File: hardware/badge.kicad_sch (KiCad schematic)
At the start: 53 parts, among them J1 SAO V.1.69bis master, Q1 BSS138, SW1 power, SW2 SW_Push, SW3 update epaper, U1 Seeed XIAO ESP32-C3, U2 MH-ET_epaper_ 2.13, U3 5V boost converter, U4 TXS0104EPWR

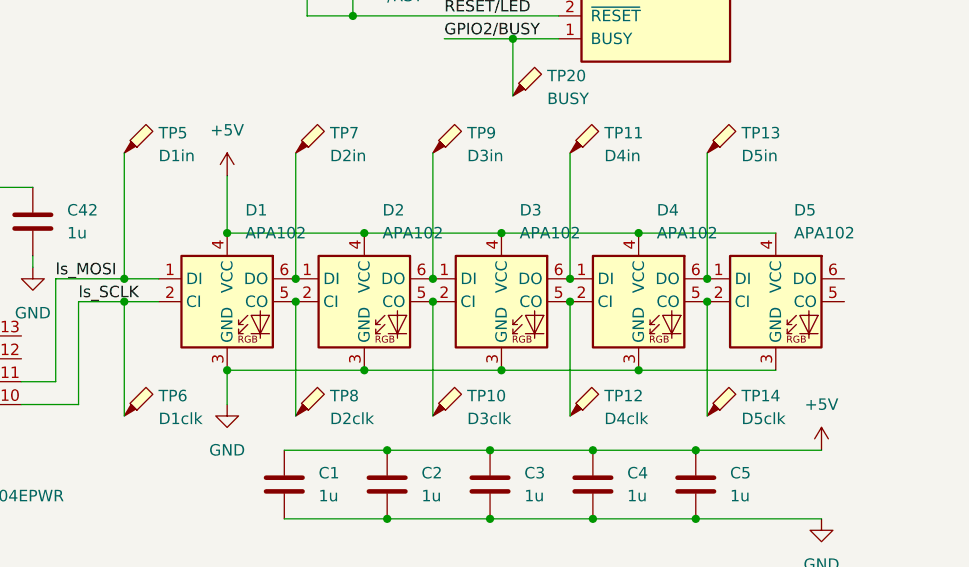
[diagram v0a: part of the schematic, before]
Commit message: fix smart LED APA102-2020, and some minor re-routings
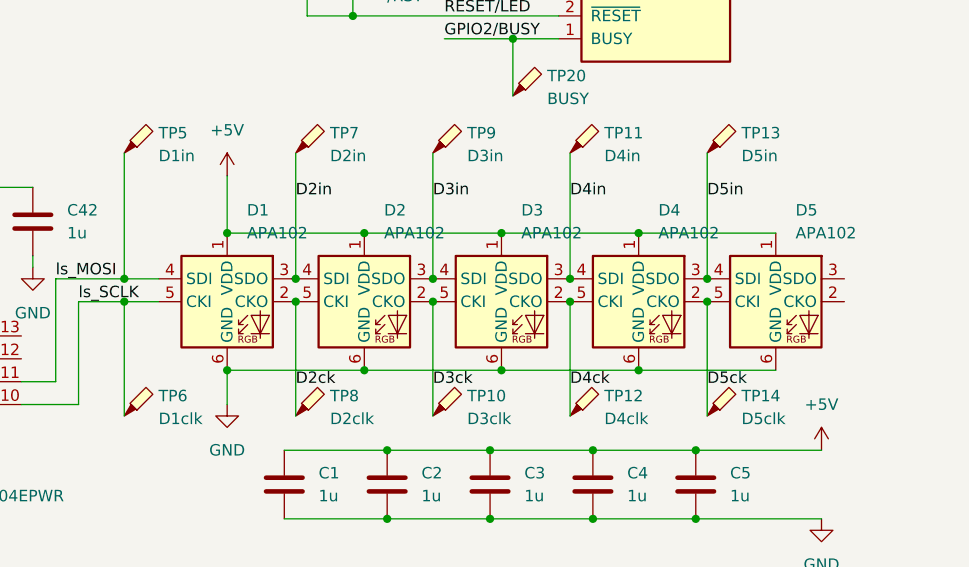
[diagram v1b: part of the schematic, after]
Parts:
- D1, D2, D3, D4, D5: footprint extra:LED-APA102-2020 -> LED_SMD:LED-APA102-2020; symbol LED:APA102 -> LED:APA102-2020
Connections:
- net +5V: now also D1.1 (VDD), D2.1 (VDD), D3.1 (VDD), D4.1 (VDD), D5.1 (VDD); no longer D1.4 (VCC), D2.4 (VCC), D3.4 (VCC), D4.4 (VCC), D5.4 (VCC)
- net GND: now also D1.6 (GND), D2.6 (GND), D3.6 (GND), D4.6 (GND), D5.6 (GND); no longer D1.3 (GND), D2.3 (GND), D3.3 (GND), D4.3 (GND), D5.3 (GND)
- net ls_MOSI: now also D1.4 (SDI); no longer D1.1 (DI)
- net ls_SCLK: now also D1.5 (CKI); no longer D1.2 (CI)
- net D5ck: now reaches D5.5 (CKI)
- net D5ck: now also D4.2 (CKO), TP14.1
- new net D2ck: D1.2 (CKO), D2.5 (CKI), TP8.1
- new net D2in: D1.3 (SDO), D2.4 (SDI), TP7.1
- new net D3ck: D2.2 (CKO), D3.5 (CKI), TP10.1
- new net D3in: D2.3 (SDO), D3.4 (SDI), TP9.1
- new net D4ck: D3.2 (CKO), D4.5 (CKI), TP12.1
- new net D4in: D3.3 (SDO), D4.4 (SDI), TP11.1
- new net D5in: D4.3 (SDO), D5.4 (SDI), TP13.1
- now unconnected: D5.2 (CI)
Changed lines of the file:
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@@
+    (effects (font (size 1.27 1.27)) (justify left bottom))
+  )
+  (label "D3ck" (at 229.87 98.425 0) (fields_autoplaced)
     (effects (font (size 1.27 1.27)) (justify left bottom))
   )
@@
     (effects (font (size 1.27 1.27)) (justify left bottom))
   )
+  (label "D2in" (at 214.63 77.47 0) (fields_autoplaced)
+    (effects (font (size 1.27 1.27)) (justify left bottom))
+  )
   (label "GPIO2{slash}BUSY" (at 266.7 135.89 0) (fields_autoplaced)
     (effects (font (size 1.27 1.27)) (justify left bottom))
@@
     (effects (font (size 1.27 1.27)) (justify left bottom))
   )
+  (label "D4ck" (at 245.11 98.425 0) (fields_autoplaced)
+    (effects (font (size 1.27 1.27)) (justify left bottom))
+  )
   (label "MOSI" (at 151.13 97.79 0) (fields_autoplaced)
     (effects (font (size 1.27 1.27)) (justify left bottom))
@@
     (effects (font (size 1.27 1.27)) (justify left bottom))
   )
+  (label "D2ck" (at 214.63 98.425 0) (fields_autoplaced)
+    (effects (font (size 1.27 1.27)) (justify left bottom))
+  )
+  (label "D5in" (at 260.35 77.47 0) (fields_autoplaced)
+    (effects (font (size 1.27 1.27)) (justify left bottom))
+  )
   (label "CS{slash}OE" (at 127 60.96 0) (fields_autoplaced)
     (effects (font (size 1.27 1.27)) (justify left bottom))
@@
     (effects (font (size 1.27 1.27)) (justify left bottom))
   )
+  (label "D4in" (at 245.11 77.47 0) (fields_autoplaced)
+    (effects (font (size 1.27 1.27)) (justify left bottom))
+  )
   (label "CS{slash}OE" (at 151.13 90.17 0) (fields_autoplaced)
     (effects (font (size 1.27 1.27)) (justify left bottom))
@@
     (effects (font (size 1.27 1.27)) (justify left bottom))
   )
+  (label "D3in" (at 229.87 77.47 0) (fields_autoplaced)
+    (effects (font (size 1.27 1.27)) (justify left bottom))
+  )
   (label "RESET{slash}LED" (at 59.69 60.96 0) (fields_autoplaced)
     (effects (font (size 1.27 1.27)) (justify left bottom))
   )
   (label "Vdark" (at 59.69 45.72 0) (fields_autoplaced)
+    (effects (font (size 1.27 1.27)) (justify left bottom))
+  )
+  (label "D5ck" (at 260.35 98.425 0) (fields_autoplaced)
     (effects (font (size 1.27 1.27)) (justify left bottom))
   )
@@
     )
   )
-  (symbol (lib_id "LED:APA102") (at 237.49 88.9 0) (unit 1)
-    (in_bom yes) (on_board yes) (dnp no) (fields_autoplaced)
-    (property "Reference" "D3" (at 239.5094 78.74 0)
-      (effects (font (size 1.27 1.27)) (justify left))
-    )
-    (property "Value" "APA102" (at 239.5094 81.28 0)
-      (effects (font (size 1.27 1.27)) (justify left))
-    )
-    (property "Footprint" "extra:LED-APA102-2020" (at 238.76 96.52 0)
+  (symbol (lib_id "LED:APA102-2020") (at 237.49 88.9 0) (unit 1)
+    (in_bom yes) (on_board yes) (dnp no) (fields_autoplaced)
+    (property "Reference" "D3" (at 239.6841 78.74 0)
+      (effects (font (size 1.27 1.27)) (justify left))
+    )
+    (property "Value" "APA102" (at 239.6841 81.28 0)
+      (effects (font (size 1.27 1.27)) (justify left))
+    )
+    (property "Footprint" "LED_SMD:LED-APA102-2020" (at 238.76 96.52 0)
       (effects (font (size 1.27 1.27)) (justify left top) hide)
     )
-    (property "Datasheet" "http://www.led-color.com/upload/201506/APA102%20LED.pdf" (at 240.03 98.425 0)
+    (property "Datasheet" "http://www.led-color.com/upload/201604/APA102-2020%20SMD%20LED.pdf" (at 240.03 98.425 0)
       (effects (font (size 1.27 1.27)) (justify left top) hide)
     )
@@
     )
   )
-  (symbol (lib_id "LED:APA102") (at 207.01 88.9 0) (unit 1)
-    (in_bom yes) (on_board yes) (dnp no) (fields_autoplaced)
-    (property "Reference" "D1" (at 209.0294 78.74 0)
-      (effects (font (size 1.27 1.27)) (justify left))
-    )
-    (property "Value" "APA102" (at 209.0294 81.28 0)
-      (effects (font (size 1.27 1.27)) (justify left))
-    )
-    (property "Footprint" "extra:LED-APA102-2020" (at 208.28 96.52 0)
+  (symbol (lib_id "LED:APA102-2020") (at 207.01 88.9 0) (unit 1)
+    (in_bom yes) (on_board yes) (dnp no) (fields_autoplaced)
+    (property "Reference" "D1" (at 209.2041 78.74 0)
+      (effects (font (size 1.27 1.27)) (justify left))
+    )
+    (property "Value" "APA102" (at 209.2041 81.28 0)
+      (effects (font (size 1.27 1.27)) (justify left))
+    )
+    (property "Footprint" "LED_SMD:LED-APA102-2020" (at 208.28 96.52 0)
       (effects (font (size 1.27 1.27)) (justify left top) hide)
     )
-    (property "Datasheet" "http://www.led-color.com/upload/201506/APA102%20LED.pdf" (at 209.55 98.425 0)
+    (property "Datasheet" "http://www.led-color.com/upload/201604/APA102-2020%20SMD%20LED.pdf" (at 209.55 98.425 0)
       (effects (font (size 1.27 1.27)) (justify left top) hide)
     )
@@
     )
   )
-  (symbol (lib_id "LED:APA102") (at 252.73 88.9 0) (unit 1)
-    (in_bom yes) (on_board yes) (dnp no) (fields_autoplaced)
-    (property "Reference" "D4" (at 254.7494 78.74 0)
-      (effects (font (size 1.27 1.27)) (justify left))
-    )
-    (property "Value" "APA102" (at 254.7494 81.28 0)
-      (effects (font (size 1.27 1.27)) (justify left))
-    )
-    (property "Footprint" "extra:LED-APA102-2020" (at 254 96.52 0)
+  (symbol (lib_id "LED:APA102-2020") (at 252.73 88.9 0) (unit 1)
+    (in_bom yes) (on_board yes) (dnp no) (fields_autoplaced)
+    (property "Reference" "D4" (at 254.9241 78.74 0)
+      (effects (font (size 1.27 1.27)) (justify left))
+    )
+    (property "Value" "APA102" (at 254.9241 81.28 0)
+      (effects (font (size 1.27 1.27)) (justify left))
+    )
+    (property "Footprint" "LED_SMD:LED-APA102-2020" (at 254 96.52 0)
       (effects (font (size 1.27 1.27)) (justify left top) hide)
     )
-    (property "Datasheet" "http://www.led-color.com/upload/201506/APA102%20LED.pdf" (at 255.27 98.425 0)
+    (property "Datasheet" "http://www.led-color.com/upload/201604/APA102-2020%20SMD%20LED.pdf" (at 255.27 98.425 0)
       (effects (font (size 1.27 1.27)) (justify left top) hide)
     )
@@
     )
   )
-  (symbol (lib_id "LED:APA102") (at 267.97 88.9 0) (unit 1)
-    (in_bom yes) (on_board yes) (dnp no) (fields_autoplaced)
-    (property "Reference" "D5" (at 269.9894 78.74 0)
-      (effects (font (size 1.27 1.27)) (justify left))
-    )
-    (property "Value" "APA102" (at 269.9894 81.28 0)
-      (effects (font (size 1.27 1.27)) (justify left))
-    )
-    (property "Footprint" "extra:LED-APA102-2020" (at 269.24 96.52 0)
+  (symbol (lib_id "LED:APA102-2020") (at 267.97 88.9 0) (unit 1)
+    (in_bom yes) (on_board yes) (dnp no) (fields_autoplaced)
+    (property "Reference" "D5" (at 270.1641 78.74 0)
+      (effects (font (size 1.27 1.27)) (justify left))
+    )
+    (property "Value" "APA102" (at 270.1641 81.28 0)
+      (effects (font (size 1.27 1.27)) (justify left))
+    )
+    (property "Footprint" "LED_SMD:LED-APA102-2020" (at 269.24 96.52 0)
       (effects (font (size 1.27 1.27)) (justify left top) hide)
     )
-    (property "Datasheet" "http://www.led-color.com/upload/201506/APA102%20LED.pdf" (at 270.51 98.425 0)
+    (property "Datasheet" "http://www.led-color.com/upload/201604/APA102-2020%20SMD%20LED.pdf" (at 270.51 98.425 0)
       (effects (font (size 1.27 1.27)) (justify left top) hide)
     )
@@
     )
   )
-  (symbol (lib_id "LED:APA102") (at 222.25 88.9 0) (unit 1)
-    (in_bom yes) (on_board yes) (dnp no) (fields_autoplaced)
-    (property "Reference" "D2" (at 224.2694 78.74 0)
-      (effects (font (size 1.27 1.27)) (justify left))
-    )
-    (property "Value" "APA102" (at 224.2694 81.28 0)
-      (effects (font (size 1.27 1.27)) (justify left))
-    )
-    (property "Footprint" "extra:LED-APA102-2020" (at 223.52 96.52 0)
+  (symbol (lib_id "LED:APA102-2020") (at 222.25 88.9 0) (unit 1)
+    (in_bom yes) (on_board yes) (dnp no) (fields_autoplaced)
+    (property "Reference" "D2" (at 224.4441 78.74 0)
+      (effects (font (size 1.27 1.27)) (justify left))
+    )
+    (property "Value" "APA102" (at 224.4441 81.28 0)
+      (effects (font (size 1.27 1.27)) (justify left))
+    )
+    (property "Footprint" "LED_SMD:LED-APA102-2020" (at 223.52 96.52 0)
       (effects (font (size 1.27 1.27)) (justify left top) hide)
     )
-    (property "Datasheet" "http://www.led-color.com/upload/201506/APA102%20LED.pdf" (at 224.79 98.425 0)
+    (property "Datasheet" "http://www.led-color.com/upload/201604/APA102-2020%20SMD%20LED.pdf" (at 224.79 98.425 0)
       (effects (font (size 1.27 1.27)) (justify left top) hide)
     )

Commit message: rename RESET/LED net to LED/RESET, for consistency with other multi-use pins
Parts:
- TP1, TP10, TP11, TP12, TP13, TP14, TP15, TP16, TP17, TP18, TP19, TP2, TP20, TP3, TP4, TP5, TP6, TP7, TP8, TP9: now left out of the parts list
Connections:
- net RESET/LED renamed LED/RESET

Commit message: rename MISO/Vbutton1 net to Vbutton1, for consistency with other single-use pins
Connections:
- net MISO/Vbutton1 renamed Vbutton1
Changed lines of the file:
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@@
 		)
 	)
-	(label "MISO{slash}Vbutton1"
+	(label "Vbutton1"
 		(at 100.33 135.89 0)
 		(fields_autoplaced yes)
@@
 		)
 	)
-	(label "MISO{slash}Vbutton1"
+	(label "Vbutton1"
 		(at 127 53.34 0)
 		(fields_autoplaced yes)

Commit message: put GND between I2C tracks, improve DRC result
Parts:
- D1, D2, D3, D4, D5: footprint LED_SMD:LED-APA102-2020 -> extra:LED-APA102-2020
- TP2: value 3.8V -> 4.1V
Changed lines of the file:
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@@
 			)
 		)
-		(property "Footprint" "LED_SMD:LED-APA102-2020"
+		(property "Footprint" "extra:LED-APA102-2020"
 			(at 238.76 96.52 0)
 			(effects
@@
 			)
 		)
-		(property "Footprint" "LED_SMD:LED-APA102-2020"
+		(property "Footprint" "extra:LED-APA102-2020"
 			(at 208.28 96.52 0)
 			(effects
@@
 			)
 		)
-		(property "Footprint" "LED_SMD:LED-APA102-2020"
+		(property "Footprint" "extra:LED-APA102-2020"
 			(at 254 96.52 0)
 			(effects
@@
 			)
 		)
-		(property "Footprint" "LED_SMD:LED-APA102-2020"
+		(property "Footprint" "extra:LED-APA102-2020"
 			(at 269.24 96.52 0)
 			(effects
@@
 			)
 		)
-		(property "Footprint" "LED_SMD:LED-APA102-2020"
+		(property "Footprint" "extra:LED-APA102-2020"
 			(at 223.52 96.52 0)
 			(effects
@@
 		(fields_autoplaced yes)
 		(property "Reference" "TP2"
-			(at 77.47 73.9775 0)
+			(at 77.47 73.3424 0)
 			(effects
 				(font
@@
 			)
 		)
-		(property "Value" "3.8V"
-			(at 77.47 76.5175 0)
+		(property "Value" "4.1V"
+			(at 77.47 75.8824 0)
 			(effects
 				(font

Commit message: put GND between SPI tracks
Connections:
- net MOSI: now also U4.5 (A4); no longer U4.4 (A3)
- net SCLK: now also U4.4 (A3); no longer U4.5 (A4)
- net ls_MOSI: now also U4.10 (B4); no longer U4.11 (B3)
- net ls_SCLK: now also U4.11 (B3); no longer U4.10 (B4)
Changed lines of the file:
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@@
+	(wire
+		(pts
+			(xy 187.96 100.33) (xy 187.96 86.36)
+		)
+		(stroke
+			(width 0)
+			(type default)
+		)
+	)
 	(wire
 		(pts
@@
 	(wire
 		(pts
+			(xy 184.15 97.79) (xy 190.5 97.79)
+		)
+		(stroke
+			(width 0)
+			(type default)
+		)
+	)
+	(wire
+		(pts
 			(xy 207.01 81.28) (xy 222.25 81.28)
 		)
@@
 	(wire
 		(pts
-			(xy 184.15 100.33) (xy 190.5 100.33)
-		)
-		(stroke
-			(width 0)
-			(type default)
-		)
-	)
-	(wire
-		(pts
 			(xy 33.02 78.74) (xy 25.4 78.74)
 		)
@@
 	(wire
 		(pts
+			(xy 184.15 100.33) (xy 187.96 100.33)
+		)
+		(stroke
+			(width 0)
+			(type default)
+		)
+	)
+	(wire
+		(pts
 			(xy 59.69 38.1) (xy 76.2 38.1)
 		)
@@
 	(wire
 		(pts
-			(xy 184.15 97.79) (xy 187.96 97.79)
-		)
-		(stroke
-			(width 0)
-			(type default)
-		)
-	)
-	(wire
-		(pts
 			(xy 231.14 44.45) (xy 243.84 44.45)
 		)
@@
 	(wire
 		(pts
-			(xy 187.96 86.36) (xy 187.96 97.79)
-		)
-		(stroke
-			(width 0)
-			(type default)
-		)
-	)
-	(wire
-		(pts
 			(xy 176.53 76.2) (xy 176.53 82.55)
 		)
@@
 	(wire
 		(pts
+			(xy 190.5 97.79) (xy 190.5 88.9)
+		)
+		(stroke
+			(width 0)
+			(type default)
+		)
+	)
+	(wire
+		(pts
 			(xy 207.01 96.52) (xy 222.25 96.52)
 		)
@@
 		(pts
 			(xy 194.31 30.48) (xy 194.31 35.56)
-		)
-		(stroke
-			(width 0)
-			(type default)
-		)
-	)
-	(wire
-		(pts
-			(xy 190.5 88.9) (xy 190.5 100.33)
 		)
 		(stroke
@@
 		)
 	)
-	(label "SCLK"
-		(at 151.13 100.33 0)
-		(fields_autoplaced yes)
-		(effects
-			(font
-				(size 1.27 1.27)
-			)
-			(justify left bottom)
-		)
-	)
 	(label "Vbutton1"
 		(at 100.33 135.89 0)
@@
 	)
 	(label "SCLK"
+		(at 151.13 97.79 0)
+		(fields_autoplaced yes)
+		(effects
+			(font
+				(size 1.27 1.27)
+			)
+			(justify left bottom)
+		)
+	)
+	(label "SCLK"
 		(at 127 57.15 0)
 		(fields_autoplaced yes)
@@
 	)
 	(label "MOSI"
-		(at 151.13 97.79 0)
-		(fields_autoplaced yes)
-		(effects
+		(at 151.13 100.33 0)
+		(fields_autoplaced yes)
+		(effects

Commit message: swap Vdark, Vmeasure CPU pins
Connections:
- net Vdark: now also U1.4 (G5_A3_D3); no longer U1.3 (G4_A2_D2)
- net Vmeasure: now also U1.3 (G4_A2_D2); no longer U1.4 (G5_A3_D3)
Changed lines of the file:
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@@
+		)
+	)
+	(label "Vdark"
+		(at 59.69 49.53 0)
+		(fields_autoplaced yes)
+		(effects
+			(font
+				(size 1.27 1.27)
+			)
+			(justify left bottom)
 		)
 	)
@@
 		)
 	)
+	(label "Vmeasure"
+		(at 59.69 45.72 0)
+		(fields_autoplaced yes)
+		(effects
+			(font
+				(size 1.27 1.27)
+			)
+			(justify left bottom)
+		)
+	)
 	(label "SCLK"
 		(at 127 57.15 0)
@@
 		)
 	)
-	(label "Vmeasure"
-		(at 59.69 49.53 0)
-		(fields_autoplaced yes)
-		(effects
-			(font
-				(size 1.27 1.27)
-			)
-			(justify left bottom)
-		)
-	)
 	(label "D2ck"
 		(at 214.63 98.425 0)
@@
 		(fields_autoplaced yes)
 		(effects
-			(font
-				(size 1.27 1.27)
-			)
-			(justify left bottom)
-		)
-	)
-	(label "Vdark"
-		(at 59.69 45.72 0)
-		(fields_autoplaced yes)
-		(effects
